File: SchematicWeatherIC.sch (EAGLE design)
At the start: 21 parts, among them U1 ESP32-C6FH4, U2 MIC5365-3.3YC5-TR

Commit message: Add files via upload
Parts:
- added R6, R7: 5.1k, rcl:R-US_VMTB60
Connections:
- new net N$12: R6.1, USB.CC1
- new net N$13: R7.1, USB.CC2
- net GND: now also R7.2
- net N$6: now also CP2102.VBUS
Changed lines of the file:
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@@
 <part name="R4" library="rcl" library_urn="urn:adsk.eagle:library:334" deviceset="R-US_" device="VMTB60" package3d_urn="urn:adsk.eagle:package:26122/2" value="220"/>
 <part name="R5" library="rcl" library_urn="urn:adsk.eagle:library:334" deviceset="R-US_" device="VMTB60" package3d_urn="urn:adsk.eagle:package:26122/2" value="220"/>
+<part name="R6" library="rcl" library_urn="urn:adsk.eagle:library:334" deviceset="R-US_" device="VMTB60" package3d_urn="urn:adsk.eagle:package:26122/2" value="5.1k"/>
+<part name="R7" library="rcl" library_urn="urn:adsk.eagle:library:334" deviceset="R-US_" device="VMTB60" package3d_urn="urn:adsk.eagle:package:26122/2" value="5.1k"/>
 </parts>
 <sheets>
@@
 <attribute name="NAME" x="19.05" y="128.4986" size="1.778" layer="95"/>
 <attribute name="VALUE" x="19.05" y="123.698" size="1.778" layer="96"/>
+</instance>
+<instance part="R6" gate="G$1" x="58.42" y="134.62" smashed="yes" rot="R270">
+<attribute name="NAME" x="59.9186" y="138.43" size="1.778" layer="95" rot="R270"/>
+<attribute name="VALUE" x="55.118" y="138.43" size="1.778" layer="96" rot="R270"/>
+</instance>
+<instance part="R7" gate="G$1" x="119.38" y="129.54" smashed="yes" rot="R270">
+<attribute name="NAME" x="120.8786" y="133.35" size="1.778" layer="95" rot="R270"/>
+<attribute name="VALUE" x="116.078" y="133.35" size="1.778" layer="96" rot="R270"/>
 </instance>
 </instances>
@@
 <wire x1="114.3" y1="96.52" x2="114.3" y2="27.94" width="0.1524" layer="91"/>
 <wire x1="124.46" y1="119.38" x2="132.08" y2="119.38" width="0.1524" layer="91"/>
-<wire x1="124.46" y1="119.38" x2="114.3" y2="119.38" width="0.1524" layer="91"/>
+<wire x1="124.46" y1="119.38" x2="119.38" y2="119.38" width="0.1524" layer="91"/>
 <junction x="124.46" y="119.38"/>
 <junction x="114.3" y="119.38"/>
 <pinref part="RGB" gate="A" pin="2"/>
+<wire x1="119.38" y1="119.38" x2="114.3" y2="119.38" width="0.1524" layer="91"/>
 <wire x1="50.8" y1="116.84" x2="66.04" y2="116.84" width="0.1524" layer="91"/>
 <wire x1="66.04" y1="116.84" x2="66.04" y2="96.52" width="0.1524" layer="91"/>
 <wire x1="66.04" y1="96.52" x2="114.3" y2="96.52" width="0.1524" layer="91"/>
 <junction x="114.3" y="96.52"/>
+<pinref part="R7" gate="G$1" pin="2"/>
+<wire x1="119.38" y1="124.46" x2="119.38" y2="119.38" width="0.1524" layer="91"/>
+<junction x="119.38" y="119.38"/>
 </segment>
 </net>
@@
 <wire x1="124.46" y1="129.54" x2="127" y2="129.54" width="0.1524" layer="91"/>
 <junction x="127" y="129.54"/>
+<wire x1="137.16" y1="129.54" x2="137.16" y2="111.76" width="0.1524" layer="91"/>
+<wire x1="137.16" y1="111.76" x2="149.86" y2="111.76" width="0.1524" layer="91"/>
+<junction x="137.16" y="129.54"/>
+<pinref part="CP2102" gate="G$1" pin="VBUS"/>
+<wire x1="149.86" y1="111.76" x2="149.86" y2="116.84" width="0.1524" layer="91"/>
 </segment>
 </net>
@@
 </segment>
 </net>
+<net name="N$12" class="0">
+<segment>
+<pinref part="USB" gate="G$1" pin="CC1"/>
+<wire x1="73.66" y1="142.24" x2="58.42" y2="142.24" width="0.1524" layer="91"/>
+<wire x1="58.42" y1="142.24" x2="58.42" y2="139.7" width="0.1524" layer="91"/>
+<pinref part="R6" gate="G$1" pin="1"/>
+</segment>
+</net>
+<net name="N$13" class="0">
+<segment>
+<pinref part="USB" gate="G$1" pin="CC2"/>
+<wire x1="109.22" y1="142.24" x2="119.38" y2="142.24" width="0.1524" layer="91"/>
+<wire x1="119.38" y1="142.24" x2="119.38" y2="134.62" width="0.1524" layer="91"/>
+<pinref part="R7" gate="G$1" pin="1"/>
+</segment>
+</net>

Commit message: finish mostly all connections except to esp32 ic
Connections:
- net GND: now also R6.2
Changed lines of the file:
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@@
 <wire x1="119.38" y1="124.46" x2="119.38" y2="119.38" width="0.1524" layer="91"/>
 <junction x="119.38" y="119.38"/>
+<pinref part="R6" gate="G$1" pin="2"/>
+<wire x1="58.42" y1="129.54" x2="58.42" y2="127" width="0.1524" layer="91"/>
+<wire x1="58.42" y1="127" x2="66.04" y2="127" width="0.1524" layer="91"/>
+<junction x="66.04" y="127"/>
 </segment>
 </net>

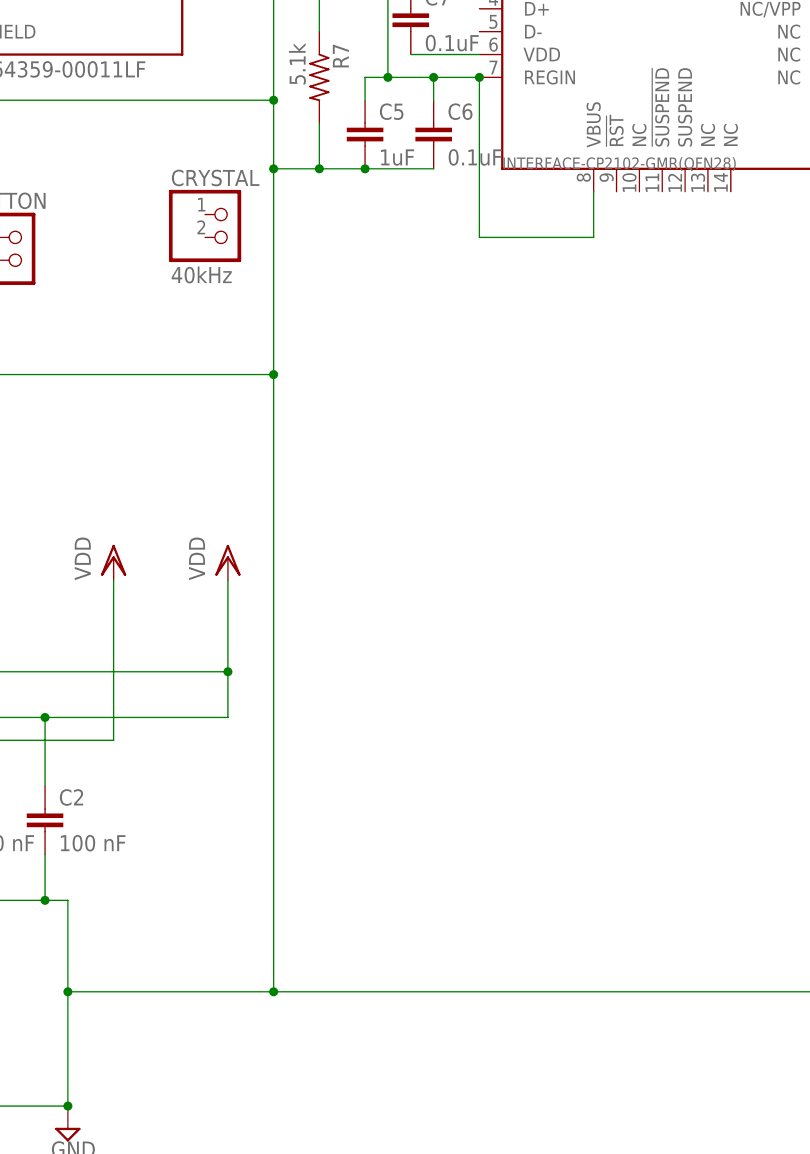
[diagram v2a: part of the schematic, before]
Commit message: add crystal connection
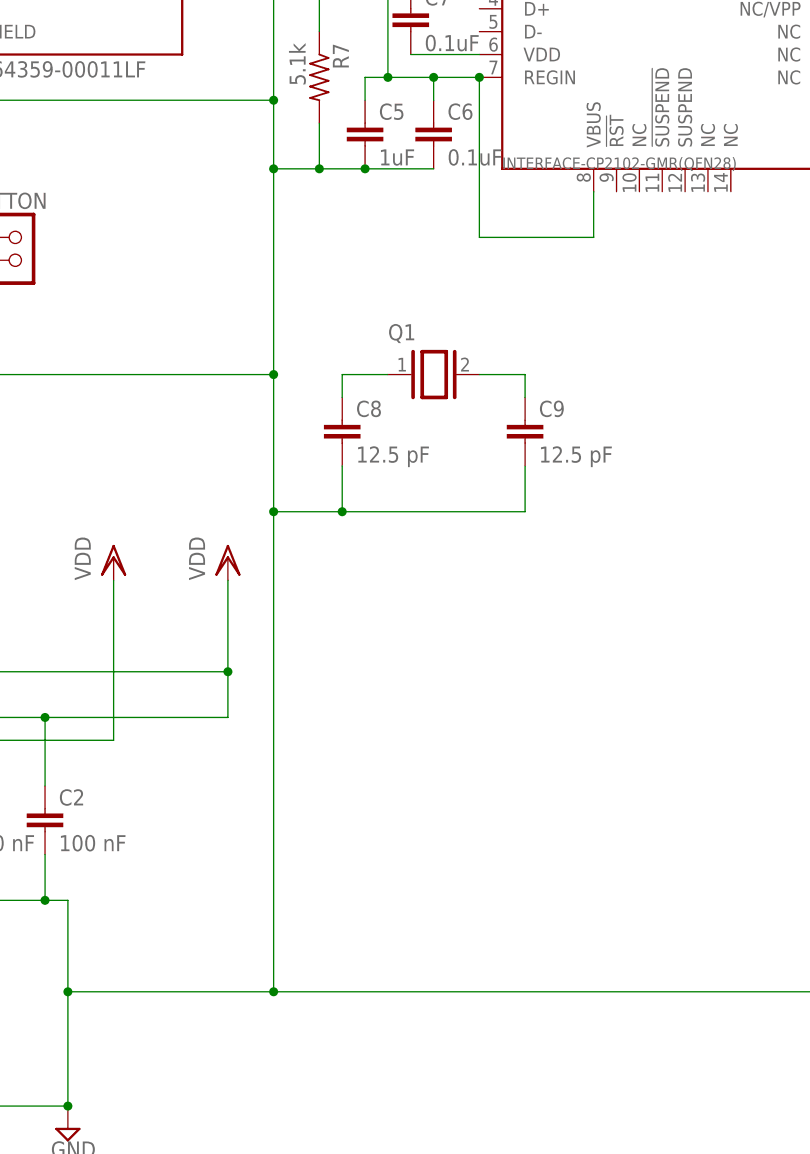
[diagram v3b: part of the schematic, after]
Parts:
- removed CRYSTAL: 40kHz, pinhead:PINHD-1X2
- added C8, C9: 12.5 pF, capacitor-wima:C5/3
- added Q1: (no value), special:XTAL/S
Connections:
- new net N$11: C8.1, Q1.1
- new net N$15: C9.1, Q1.2
- net GND: now also C8.2, C9.2
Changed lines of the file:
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@@
 <part name="LCD" library="pinhead" library_urn="urn:adsk.eagle:library:325" deviceset="PINHD-1X4" device="" package3d_urn="urn:adsk.eagle:package:22407/2"/>
 <part name="BUTTON" library="pinhead" library_urn="urn:adsk.eagle:library:325" deviceset="PINHD-1X2" device="" package3d_urn="urn:adsk.eagle:package:22435/2"/>
-<part name="CRYSTAL" library="pinhead" library_urn="urn:adsk.eagle:library:325" deviceset="PINHD-1X2" device="" package3d_urn="urn:adsk.eagle:package:22435/2" value="40kHz"/>
 <part name="U2" library="MIC5365-3.3YC5-TR" deviceset="MIC5365-3.3YC5-TR" device=""/>
 <part name="CP2102" library="INTERFACE-CP2102-GMR_QFN28_" deviceset="INTERFACE-CP2102-GMR(QFN28)" device=""/>
@@
 <part name="R6" library="rcl" library_urn="urn:adsk.eagle:library:334" deviceset="R-US_" device="VMTB60" package3d_urn="urn:adsk.eagle:package:26122/2" value="5.1k"/>
 <part name="R7" library="rcl" library_urn="urn:adsk.eagle:library:334" deviceset="R-US_" device="VMTB60" package3d_urn="urn:adsk.eagle:package:26122/2" value="5.1k"/>
+<part name="Q1" library="special" library_urn="urn:adsk.eagle:library:367" deviceset="XTAL/S" device="" package3d_urn="urn:adsk.eagle:package:26647/2"/>
+<part name="C8" library="capacitor-wima" library_urn="urn:adsk.eagle:library:116" deviceset="C" device="5/3" package3d_urn="urn:adsk.eagle:package:5433/1" value="12.5 pF"/>
+<part name="C9" library="capacitor-wima" library_urn="urn:adsk.eagle:library:116" deviceset="C" device="5/3" package3d_urn="urn:adsk.eagle:package:5433/1" value="12.5 pF"/>
 </parts>
 <sheets>
@@
 <attribute name="VALUE" x="80.01" y="104.14" size="1.778" layer="96"/>
 </instance>
-<instance part="CRYSTAL" gate="G$1" x="109.22" y="111.76" smashed="yes">
-<attribute name="NAME" x="102.87" y="117.475" size="1.778" layer="95"/>
-<attribute name="VALUE" x="102.87" y="106.68" size="1.778" layer="96"/>
-</instance>
 <instance part="U2" gate="G$1" x="17.78" y="91.44" smashed="yes">
 <attribute name="NAME" x="7.62" y="97.79" size="1.778" layer="95"/>
@@
 <attribute name="NAME" x="120.8786" y="133.35" size="1.778" layer="95" rot="R270"/>
 <attribute name="VALUE" x="116.078" y="133.35" size="1.778" layer="96" rot="R270"/>
+</instance>
+<instance part="Q1" gate="G$1" x="132.08" y="96.52" smashed="yes">
+<attribute name="NAME" x="127" y="100.33" size="1.778" layer="95"/>
+<attribute name="VALUE" x="127" y="91.44" size="1.778" layer="96"/>
+</instance>
+<instance part="C8" gate="G$1" x="121.92" y="91.44" smashed="yes">
+<attribute name="NAME" x="123.444" y="91.821" size="1.778" layer="95"/>
+<attribute name="VALUE" x="123.444" y="86.741" size="1.778" layer="96"/>
+</instance>
+<instance part="C9" gate="G$1" x="142.24" y="91.44" smashed="yes">
+<attribute name="NAME" x="143.764" y="91.821" size="1.778" layer="95"/>
+<attribute name="VALUE" x="143.764" y="86.741" size="1.778" layer="96"/>
 </instance>
 </instances>
@@
 <pinref part="C6" gate="G$1" pin="2"/>
 <wire x1="114.3" y1="119.38" x2="114.3" y2="96.52" width="0.1524" layer="91"/>
-<wire x1="114.3" y1="96.52" x2="114.3" y2="27.94" width="0.1524" layer="91"/>
+<wire x1="114.3" y1="96.52" x2="114.3" y2="81.28" width="0.1524" layer="91"/>
+<wire x1="114.3" y1="81.28" x2="114.3" y2="27.94" width="0.1524" layer="91"/>
 <wire x1="124.46" y1="119.38" x2="132.08" y2="119.38" width="0.1524" layer="91"/>
 <wire x1="124.46" y1="119.38" x2="119.38" y2="119.38" width="0.1524" layer="91"/>
@@
 <wire x1="58.42" y1="127" x2="66.04" y2="127" width="0.1524" layer="91"/>
 <junction x="66.04" y="127"/>
+<pinref part="C8" gate="G$1" pin="2"/>
+<wire x1="121.92" y1="86.36" x2="121.92" y2="81.28" width="0.1524" layer="91"/>
+<wire x1="121.92" y1="81.28" x2="142.24" y2="81.28" width="0.1524" layer="91"/>
+<pinref part="C9" gate="G$1" pin="2"/>
+<wire x1="142.24" y1="81.28" x2="142.24" y2="86.36" width="0.1524" layer="91"/>
+<wire x1="121.92" y1="81.28" x2="114.3" y2="81.28" width="0.1524" layer="91"/>
+<junction x="121.92" y="81.28"/>
+<junction x="114.3" y="81.28"/>
 </segment>
 </net>
@@
 </segment>
 </net>
+<net name="N$11" class="0">
+<segment>
+<pinref part="Q1" gate="G$1" pin="1"/>
+<wire x1="127" y1="96.52" x2="121.92" y2="96.52" width="0.1524" layer="91"/>
+<pinref part="C8" gate="G$1" pin="1"/>
+<wire x1="121.92" y1="96.52" x2="121.92" y2="93.98" width="0.1524" layer="91"/>
+</segment>
+</net>
+<net name="N$15" class="0">
+<segment>
+<pinref part="C9" gate="G$1" pin="1"/>
+<pinref part="Q1" gate="G$1" pin="2"/>
+<wire x1="142.24" y1="93.98" x2="142.24" y2="96.52" width="0.1524" layer="91"/>
+<wire x1="142.24" y1="96.52" x2="137.16" y2="96.52" width="0.1524" layer="91"/>
+</segment>
+</net>
